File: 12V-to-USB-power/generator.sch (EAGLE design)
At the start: 62 parts, among them IC1 MC34063AD, K1 ARK500/2, K2 ARK500/2, K3 ARK500/2, K4 ARK500/2, K5 ARK500/2, K6 HEAT_NPN, K7 ARK500/2, K8 ARK500/2, Q1 IRF3704S, Q2 IRF3704S, T1 BC807, T2 BC807, X1 CV_LED, X2 PWR_LED, X3 5V_SW, X4 5V_LED, X5 5V_OUT

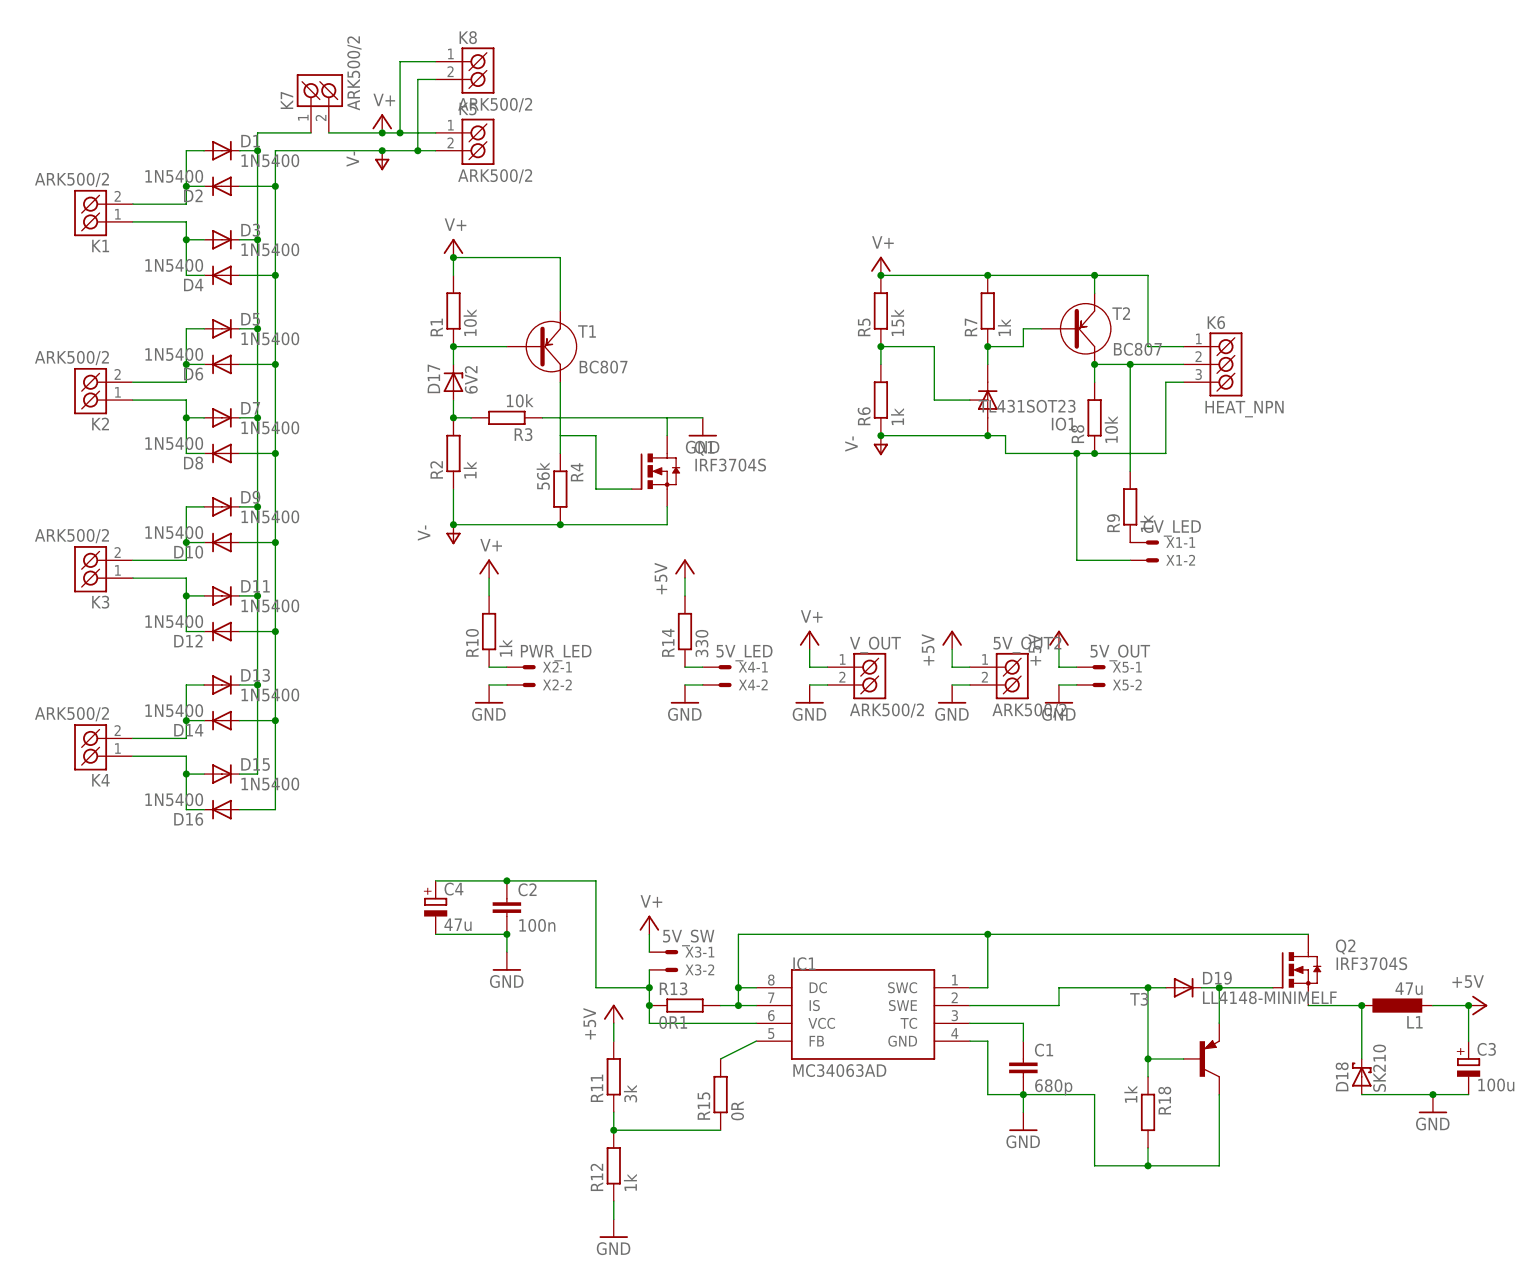
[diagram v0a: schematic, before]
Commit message: Added 12V to 5V switching regulator with MC34063 and MOSFET.
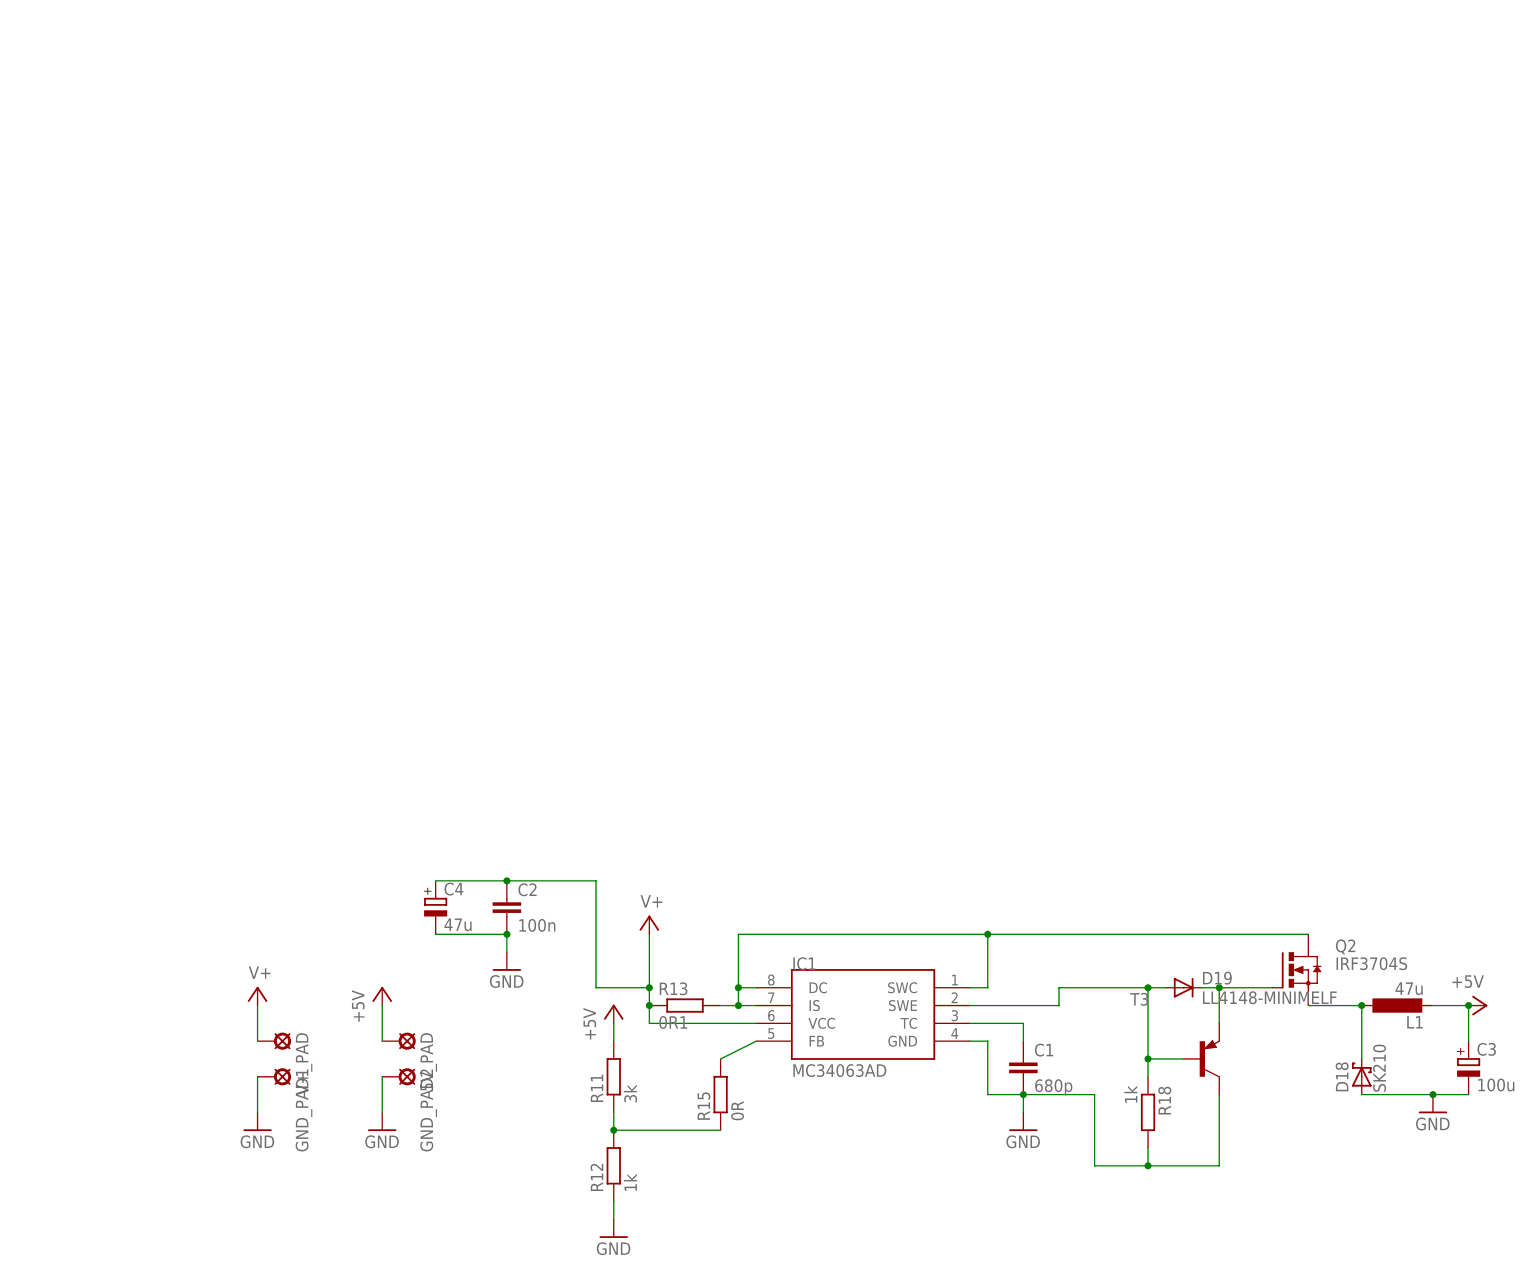
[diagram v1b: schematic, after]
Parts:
- removed 5V_OUT2, K1, K2, K3, K4, K5, K7, K8, V_OUT: ARK500/2, #PaJa_konektory:ARK500/2
- removed D1, D10, D11, D12, D13, D14, D15, D16, D2, D3, D4, D5, D6, D7, D8, D9: 1N5400, diode:1N5400
- removed D17: 6V2, diode:ZENER-DIODESOD80C
- removed IO1: TL431SOT23, references:TL431SOT23
- removed K6: HEAT_NPN, #PaJa_konektory:ARK500/3
- removed Q1: IRF3704S, transistor-power:IRF3704S
- removed R1, R3, R8: 10k, rcl:R-EU_R0805
- removed R10, R2, R6, R7, R9: 1k, rcl:R-EU_R0805
- removed R14: 330, rcl:R-EU_R0805
- removed R4: 56k, rcl:R-EU_R0805
- removed R5: 15k, rcl:R-EU_R0805
- removed T1, T2: BC807, #PaJa_30:BC807
- removed X1: CV_LED, con-molex:22-23-2021
- removed X2: PWR_LED, con-molex:22-23-2021
- removed X3: 5V_SW, con-molex:22-23-2021
- removed X4: 5V_LED, con-molex:22-23-2021
- removed X5: 5V_OUT, con-molex:22-23-2021
- added 5V_PAD, GND_PAD1, GND_PAD2, V+_PAD: LSP10, solpad:LSP10
- C4: device rcl:CPOL-EUD -> rcl:CPOL-EUE3.5-10
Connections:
- removed net N$1: D1.A, D2.C, K1.K2
- removed net N$10: D11.A, D12.C, K3.K1
- removed net N$12: IO1.R, R5.1, R6.2
- removed net N$13: D13.A, D14.C, K4.K2
- removed net N$14: D15.A, D16.C, K4.K1
- removed net N$17: D17.C, R1.1, T1.B
- removed net N$18: D17.A, R2.2, R3.2
- removed net N$2: D3.A, D4.C, K1.K1
- removed net N$20: D1.C, D11.C, D13.C, D15.C, D3.C, D5.C, D7.C, D9.C, K7.K1
- removed net N$22: R14.1, X4-1.S
- removed net N$23: R10.1, X2-1.S
- removed net N$24: C2.1, C4.+, IC1.VCC, R13.1, X3-2.S
- removed net N$3: IO1.C, R7.1, T2.B
- removed net N$4: Q1.G, R4.1, T1.C
- removed net N$5: D5.A, D6.C, K2.K2
- removed net N$6: D7.A, D8.C, K2.K1
- removed net N$7: K6.K2, R8.2, R9.2, T2.C
- removed net N$8: R9.1, X1-1.S
- removed net N$9: D10.C, D9.A, K3.K2
- removed net V-: D10.A, D12.A, D14.A, D16.A, D2.A, D4.A, D6.A, D8.A, IO1.A, K5.K2, K6.K3, K8.K2, Q1.S, R2.1, R4.2, R6.1, R8.1, X1-2.S
- net +5V: now also 5V_PAD.MP; no longer 5V_OUT2.K1, R14.2, X5-1.S
- net GND: now also GND_PAD1.MP, GND_PAD2.MP; no longer 5V_OUT2.K2, Q1.D, R3.1, V_OUT.K2, X2-2.S, X4-2.S, X5-2.S
- net V+: now also C2.1, C4.+, IC1.VCC, R13.1, V+_PAD.MP; no longer K5.K1, K6.K1, K7.K2, K8.K1, R1.2, R10.2, R5.2, R7.2, T1.E, T2.E, V_OUT.K1, X3-1.S
